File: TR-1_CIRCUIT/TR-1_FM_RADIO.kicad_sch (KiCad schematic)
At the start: 1 part

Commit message: Finalized circuit design + README
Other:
- sheet POWER_STAGE ports: added V_AMP; removed none
- sheet RADIO_AUDIO ports: added V_AMP; removed none
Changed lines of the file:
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@@
+	(wire
+		(pts
+			(xy 90.17 93.98) (xy 90.17 49.53)
+		)
+		(stroke
+			(width 0)
+			(type default)
+		)
+	)
 	(wire
 		(pts
@@
 	(wire
 		(pts
+			(xy 102.87 93.98) (xy 90.17 93.98)
+		)
+		(stroke
+			(width 0)
+			(type default)
+		)
+	)
+	(wire
+		(pts
 			(xy 95.25 78.74) (xy 95.25 68.58)
 		)
@@
 		(pts
 			(xy 73.66 105.41) (xy 72.39 105.41)
+		)
+		(stroke
+			(width 0)
+			(type default)
+		)
+	)
+	(wire
+		(pts
+			(xy 90.17 49.53) (xy 53.34 49.53)
 		)
 		(stroke
@@
 	(sheet
 		(at 102.87 86.36)
-		(size 16.51 7.62)
+		(size 16.51 10.16)
 		(exclude_from_sim no)
 		(in_bom yes)
@@
 		)
 		(property "Sheetfile" "Radio_Audio.kicad_sch"
-			(at 102.87 94.5646 0)
+			(at 102.87 97.1046 0)
 			(effects
 				(font
@@
 		(pin "RDA_SDA" input
 			(at 102.87 88.9 180)
+			(effects
+				(font
+					(size 1.27 1.27)
+				)
+				(justify left)
+			)
+		)
+		(pin "V_AMP" input
+			(at 102.87 93.98 180)
 			(effects
 				(font
@@
 	(sheet
 		(at 36.83 41.91)
-		(size 16.51 7.62)
+		(size 16.51 10.16)
 		(exclude_from_sim no)
 		(in_bom yes)
@@
 		)
 		(property "Sheetfile" "Power_Stage.kicad_sch"
-			(at 36.83 50.1146 0)
+			(at 36.83 52.6546 0)
 			(effects
 				(font
@@
 			(effects
 				(font
+					(size 1.27 1.27)
+				)
+				(justify right)
+			)
+		)
+		(pin "V_AMP" input
+			(at 53.34 49.53 0)
+			(effects
+				(font

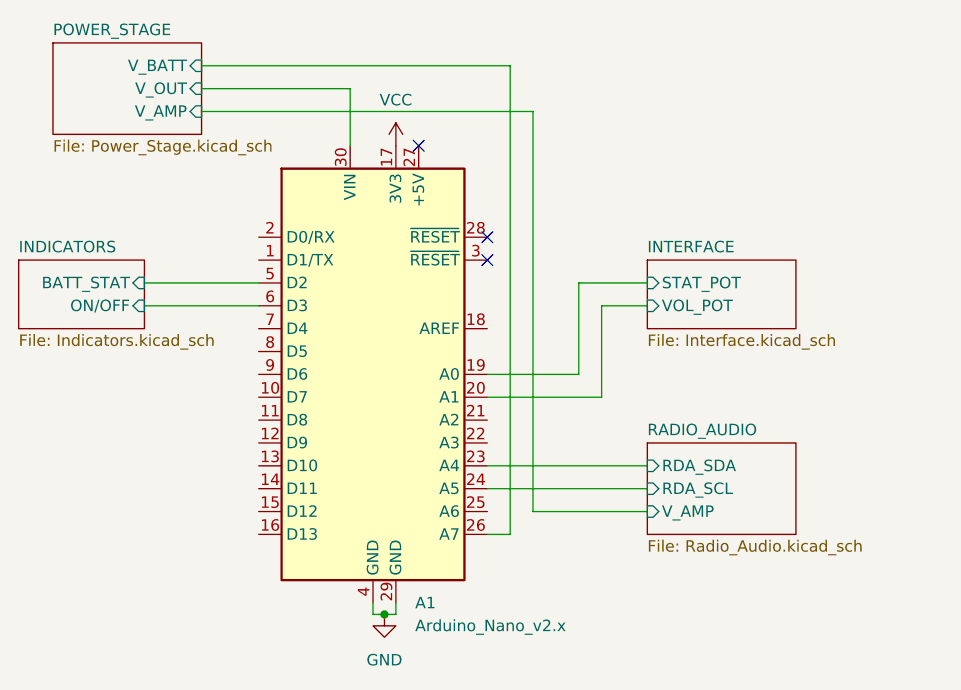
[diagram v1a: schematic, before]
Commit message: finished the overall design and swapped out the pot for an encoder
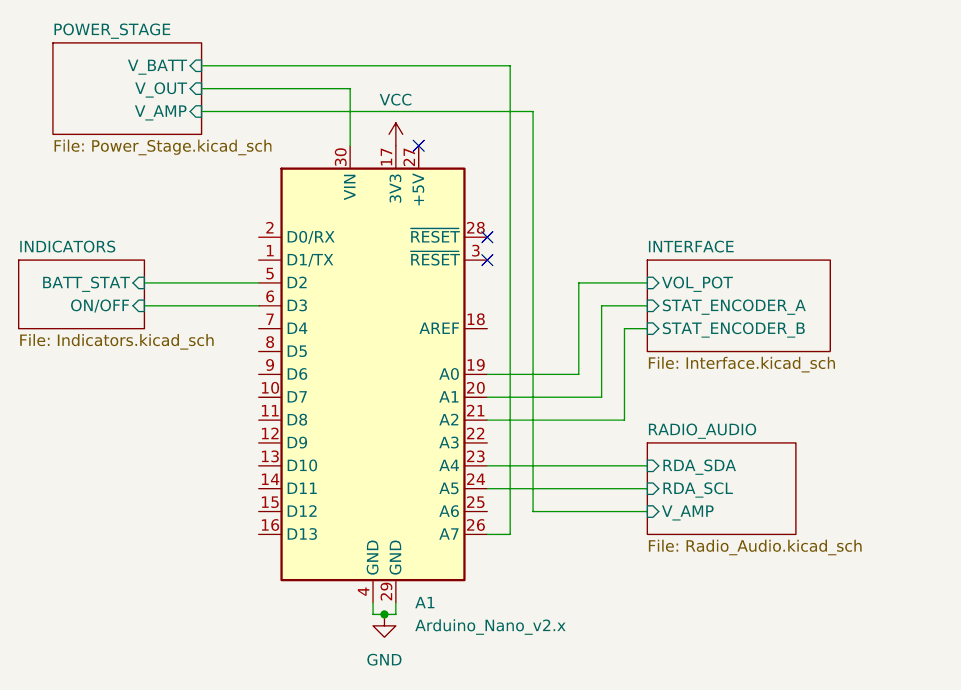
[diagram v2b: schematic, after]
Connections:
- net INTERFACE/STAT_POT is gone; now on net INTERFACE/VOL_POT: A1.19 (A0)
- net INTERFACE/VOL_POT: no longer A1.20 (A1)
- net INTERFACE/STAT_ENCODER_B: now reaches A1.21 (A2)
- new net INTERFACE/STAT_ENCODER_A: A1.20 (A1)
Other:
- sheet INTERFACE ports: added STAT_ENCODER_A, STAT_ENCODER_B; removed STAT_POT
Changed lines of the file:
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@@
+	(wire
+		(pts
+			(xy 100.33 73.66) (xy 100.33 83.82)
+		)
+		(stroke
+			(width 0)
+			(type default)
+		)
+	)
 	(wire
 		(pts
@@
 	(wire
 		(pts
+			(xy 102.87 73.66) (xy 100.33 73.66)
+		)
+		(stroke
+			(width 0)
+			(type default)
+		)
+	)
+	(wire
+		(pts
 			(xy 95.25 78.74) (xy 95.25 68.58)
 		)
@@
 		(pts
 			(xy 97.79 81.28) (xy 85.09 81.28)
+		)
+		(stroke
+			(width 0)
+			(type default)
+		)
+	)
+	(wire
+		(pts
+			(xy 100.33 83.82) (xy 85.09 83.82)
 		)
 		(stroke
@@
 	(sheet
 		(at 102.87 66.04)
-		(size 16.51 7.62)
+		(size 20.32 10.16)
 		(exclude_from_sim no)
 		(in_bom yes)
@@
 		)
 		(property "Sheetfile" "Interface.kicad_sch"
-			(at 102.87 74.2446 0)
+			(at 102.87 76.7846 0)
 			(effects
 				(font
@@
 			)
 		)
-		(pin "STAT_POT" input
+		(pin "VOL_POT" input
 			(at 102.87 68.58 180)
 			(effects
@@
 			)
 		)
-		(pin "VOL_POT" input
+		(pin "STAT_ENCODER_A" input
 			(at 102.87 71.12 180)
 			(effects
 				(font
+					(size 1.27 1.27)
+				)
+				(justify left)
+			)
+		)
+		(pin "STAT_ENCODER_B" input
+			(at 102.87 73.66 180)
+			(effects
+				(font
